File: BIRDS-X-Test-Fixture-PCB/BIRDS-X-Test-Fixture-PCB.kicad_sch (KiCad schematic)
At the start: 0 parts

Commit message: Done test fixture schematic
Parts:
- added D201, D202: LED, LED_SMD:LED_0603_1608Metric, symbol Device:LED
- added H101, H102, H103, H104, H105, H106, H107: MountingHole_Pad, symbol Mechanical:MountingHole_Pad
- added J101 (x2): ~, Connector_PinHeader_2.00mm:PinHeader_2x25_P2.00mm_Vertical, symbol Connector_Generic:Conn_02x25_Odd_Even
- added J101: LPC-50M2LG, Connector_PinHeader_2.00mm:PinHeader_2x25_P2.00mm_Horizontal, symbol Connector_Generic:Conn_02x25_Odd_Even
- added J102, J109: Conn_01x05, symbol Connector_Generic:Conn_01x05
- added J105, J106, J107, J108: Screw_Terminal_01x02, symbol Connector:Screw_Terminal_01x02
- added J110, J111: Conn_02x05_Odd_Even, symbol Connector_Generic:Conn_02x05_Odd_Even
- added JP101: Jumper_3_Open, symbol Jumper:Jumper_3_Open
- added R203: 1k, Resistor_SMD:R_0603_1608Metric_Pad0.98x0.95mm_HandSolder, symbol Device:R
- added R204: 2.2k, Resistor_SMD:R_0603_1608Metric_Pad0.98x0.95mm_HandSolder, symbol Device:R
- added SW101, SW102: SW_SPDT, symbol Switch:SW_SPDT
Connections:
- new net: JP101.2 (C), SW101.1 (A), SW102.1 (A)
- new net: D201.2 (A), R203.2
- new net: D202.2 (A), R204.2
- new net +3V3: H104.1, H105.1, J101.25 (Pin_25), J101.25 (Pin_25), J101.25 (Pin_25), J101.26 (Pin_26), J101.26 (Pin_26), J101.26 (Pin_26), J102.5 (Pin_5), J105.2 (Pin_2), J106.2 (Pin_2), J109.5 (Pin_5), J110.7 (Pin_7), J110.8 (Pin_8), J111.7 (Pin_7), J111.8 (Pin_8), JP101.1 (A), R203.1
- new net +5V: H106.1, H107.1, J101.15 (Pin_15), J101.15 (Pin_15), J101.15 (Pin_15), J101.16 (Pin_16), J101.16 (Pin_16), J101.16 (Pin_16), J102.3 (Pin_3), J107.2 (Pin_2), J108.2 (Pin_2), J109.3 (Pin_3), J110.10 (Pin_10), J110.9 (Pin_9), J111.10 (Pin_10), J111.9 (Pin_9), JP101.3 (B), R204.1
- new net DIO1_3V3_EN_FROM_BOSS: J101.19 (Pin_19), J101.19 (Pin_19), J101.19 (Pin_19), SW101.2 (B)
- new net DIO2_5V_EN_FROM_BOSS: J101.20 (Pin_20), J101.20 (Pin_20), J101.20 (Pin_20), SW102.2 (B)
- new net GND: D201.1 (K), D202.1 (K), H101.1, H102.1, H103.1, J101.13 (Pin_13), J101.13 (Pin_13), J101.13 (Pin_13), J101.14 (Pin_14), J101.14 (Pin_14), J101.14 (Pin_14), J102.4 (Pin_4), J105.1 (Pin_1), J106.1 (Pin_1), J107.1 (Pin_1), J108.1 (Pin_1), J109.4 (Pin_4), J110.5 (Pin_5), J110.6 (Pin_6), J111.5 (Pin_5), J111.6 (Pin_6), SW101.3 (C), SW102.3 (C)
- new net ST_RST: J101.3 (Pin_3), J101.3 (Pin_3), J101.3 (Pin_3), J110.1 (Pin_1), J111.1 (Pin_1)
- new net ST_SWDCLK: J101.2 (Pin_2), J101.2 (Pin_2), J101.2 (Pin_2), J110.2 (Pin_2), J111.2 (Pin_2)
- new net ST_SWDIO: J101.1 (Pin_1), J101.1 (Pin_1), J101.1 (Pin_1), J110.4 (Pin_4), J111.4 (Pin_4)
- new net SUP_3V3_1: J101.49 (Pin_49), J101.49 (Pin_49), J101.49 (Pin_49), J101.50 (Pin_50), J101.50 (Pin_50), J101.50 (Pin_50)
- new net SUP_UNREG_1: J101.23 (Pin_23), J101.23 (Pin_23), J101.23 (Pin_23), J101.24 (Pin_24), J101.24 (Pin_24), J101.24 (Pin_24)
- new net SUP_UNREG_2: J101.35 (Pin_35), J101.35 (Pin_35), J101.35 (Pin_35), J101.36 (Pin_36), J101.36 (Pin_36), J101.36 (Pin_36)
- new net UART_RX_BOSS_TO_JASPER: J101.17 (Pin_17), J101.17 (Pin_17), J101.17 (Pin_17), J102.2 (Pin_2), J109.2 (Pin_2)
- new net UART_TX_JASPER_TO_BOSS: J101.18 (Pin_18), J101.18 (Pin_18), J101.18 (Pin_18), J102.1 (Pin_1), J109.1 (Pin_1)
- no-connect marks 0 -> 95
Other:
- note added: "3-Pin Programming via Main Header: 1 - PROG_DBG_1 -> ST_SWDIO 2 - PROG_DBG_2 -> ST_SWDCLK 3 - PROG_DBG_3 -> ST_RST"
- note added: "BOSS is on USART2"
- note added: "GND is lablled as GND_SYS pin in ICD"
- note added: "On payload PCB, with connector on left side, top-down, Pin 1 is top-right corner"
- note added: "Registration Chunk on Even Side"
- note added: "Select one of these on Digikey NRPN252PARN-RC or LPC-50M2LG (2mm pitch)"
- note added: "Use SUP_3V3_2 as main power, per ICD"

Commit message: Layout and label PCB
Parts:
- added C401: 100n, Capacitor_SMD:C_1206_3216Metric_Pad1.33x1.80mm_HandSolder, symbol Device:C
- added H1, H2, H3, H4: MountingHole, MountingHole:MountingHole_4mm, symbol Mechanical:MountingHole
- added J105: Conn_01x06, Connector_PinHeader_2.54mm:PinHeader_1x06_P2.54mm_Vertical, symbol Connector_Generic:Conn_01x06
- added SW401: SW_Push, Button_Switch_THT:SW_PUSH_6mm, symbol Switch:SW_Push
- D201, D202: footprint LED_SMD:LED_0603_1608Metric -> LED_SMD:LED_1206_3216Metric_Pad1.42x1.75mm_HandSolder
- H_3V3_1: renamed from H104; footprint (none) -> MountingHole:MountingHole_4mm_Pad_Via
- H_3V3_2: renamed from H105; footprint (none) -> MountingHole:MountingHole_4mm_Pad_Via
- H_5V_1: renamed from H106; footprint (none) -> MountingHole:MountingHole_4mm_Pad_Via
- H_5V_2: renamed from H107; footprint (none) -> MountingHole:MountingHole_4mm_Pad_Via
- H_GND_1: renamed from H101; footprint (none) -> MountingHole:MountingHole_4mm_Pad_Via
- H_GND_2: renamed from H102; footprint (none) -> MountingHole:MountingHole_4mm_Pad_Via
- H_GND_3: renamed from H103; footprint (none) -> MountingHole:MountingHole_4mm_Pad_Via
- J101: footprint Connector_PinHeader_2.00mm:PinHeader_2x25_P2.00mm_Vertical -> Connector_PinHeader_2.54mm:PinHeader_2x25_P2.54mm_Vertical
- J102, J109: footprint (none) -> Connector_PinHeader_2.54mm:PinHeader_1x05_P2.54mm_Vertical
- J110, J111: footprint (none) -> Connector_IDC:IDC-Header_2x05_P2.54mm_Latch_Vertical
- JP101: footprint (none) -> Connector_PinHeader_2.54mm:PinHeader_1x03_P2.54mm_Vertical
- J_3V3_1: renamed from J105; footprint (none) -> TerminalBlock:TerminalBlock_bornier-2_P5.08mm
- J_3V3_2: renamed from J106; footprint (none) -> TerminalBlock:TerminalBlock_bornier-2_P5.08mm
- J_5V_1: renamed from J107; footprint (none) -> TerminalBlock:TerminalBlock_bornier-2_P5.08mm
- J_5V_2: renamed from J108; footprint (none) -> TerminalBlock:TerminalBlock_bornier-2_P5.08mm
- R203, R204: footprint Resistor_SMD:R_0603_1608Metric_Pad0.98x0.95mm_HandSolder -> Resistor_THT:R_Axial_DIN0411_L9.9mm_D3.6mm_P12.70mm_Horizontal
- SW_3V3_EN_DIO1: renamed from SW101; footprint (none) -> Button_Switch_THT:SW_Slide_1P2T_CK_OS102011MS2Q
- SW_5V_EN_DIO2: renamed from SW102; footprint (none) -> Button_Switch_THT:SW_Slide_1P2T_CK_OS102011MS2Q
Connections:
- net +3V3: now also J105.1 (Pin_1), J105.4 (Pin_4)
- net DIO1_3V3_EN_FROM_BOSS: now also J105.2 (Pin_2)
- net DIO2_5V_EN_FROM_BOSS: now also J105.5 (Pin_5)
- net GND: now also C401.2, J105.3 (Pin_3), J105.6 (Pin_6), SW401.1
- net ST_RST: now also C401.1, SW401.2
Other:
- note added: "Registration Chunk on Odd Side"
- note added: "Reset Button"
- note removed: "Registration Chunk on Even Side"
- moved on the sheet: J110, J111, J_3V3_1, J_3V3_2, J_5V_1, J_5V_2

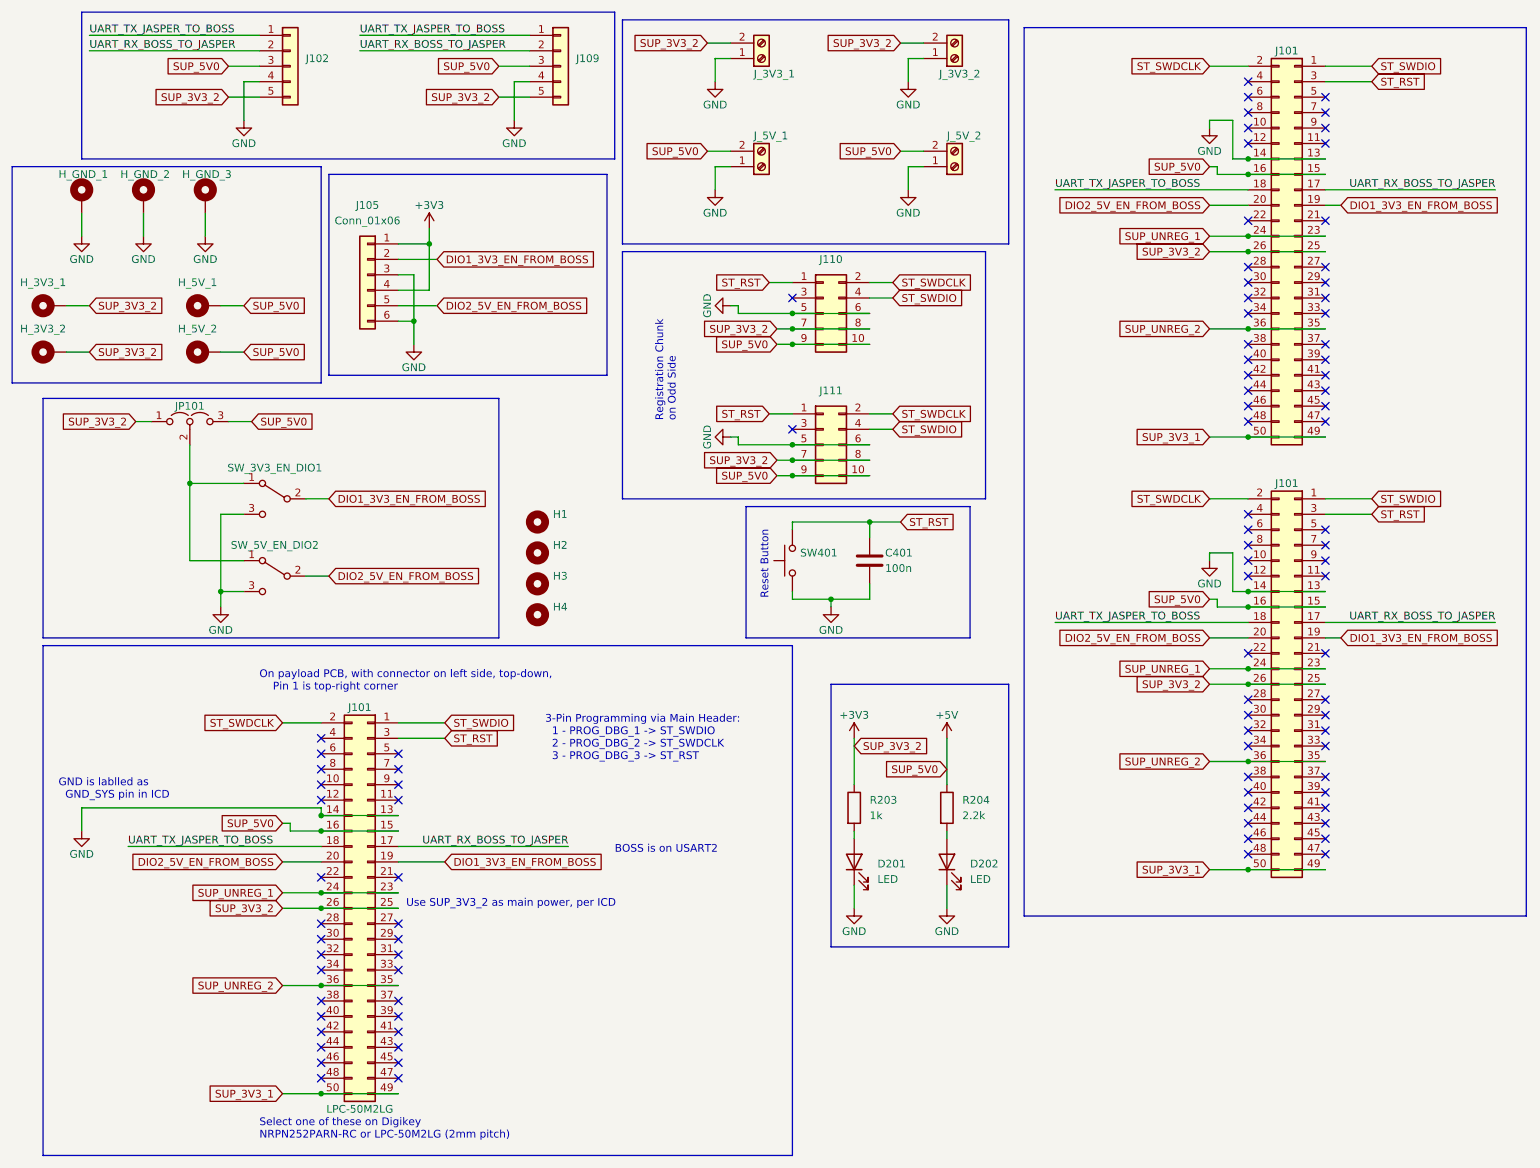
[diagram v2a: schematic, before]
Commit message: Finish test fixture
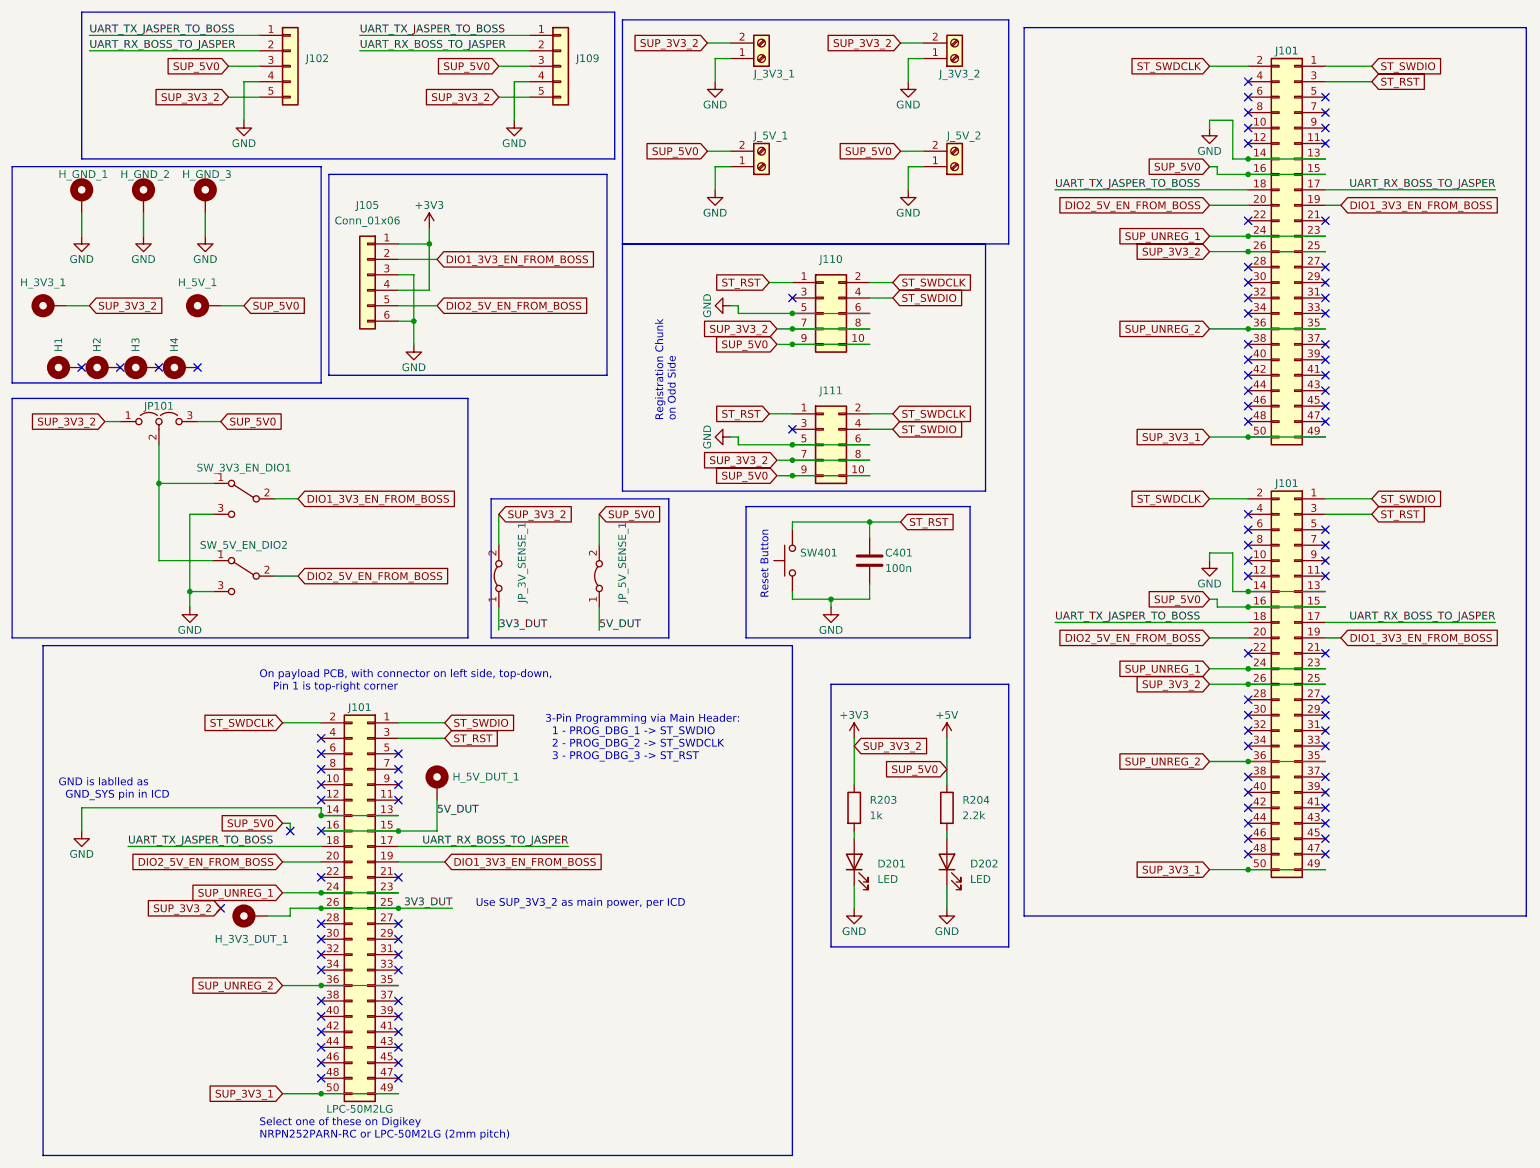
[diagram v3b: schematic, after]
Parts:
- removed H_3V3_2, H_5V_2: MountingHole_Pad, MountingHole:MountingHole_4mm_Pad_Via, symbol Mechanical:MountingHole_Pad
- added H_3V3_DUT_1, H_5V_DUT_1: MountingHole_Pad, MountingHole:MountingHole_4mm_Pad_Via, symbol Mechanical:MountingHole_Pad
- added JP_3V_SENSE_1, JP_5V_SENSE_1: Jumper_2_Bridged, TestPoint:TestPoint_2Pads_Pitch2.54mm_Drill0.8mm, symbol Jumper:Jumper_2_Bridged
- H1, H2, H3, H4: footprint MountingHole:MountingHole_4mm -> MountingHole:MountingHole_4mm_Pad; symbol Mechanical:MountingHole -> Mechanical:MountingHole_Pad
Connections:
- net +3V3: now also JP_3V_SENSE_1.2 (B); no longer J101.25 (Pin_25), J101.26 (Pin_26)
- net +5V: now also JP_5V_SENSE_1.2 (B); no longer J101.15 (Pin_15), J101.16 (Pin_16)
- new net 3V3_DUT: H_3V3_DUT_1.1, J101.25 (Pin_25), J101.26 (Pin_26), JP_3V_SENSE_1.1 (A)
- new net 5V_DUT: H_5V_DUT_1.1, J101.15 (Pin_15), J101.16 (Pin_16), JP_5V_SENSE_1.1 (A)
- no-connect marks 95 -> 102
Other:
- note removed: "BOSS is on USART2"
- moved on the sheet: JP101, SW_3V3_EN_DIO1, SW_5V_EN_DIO2

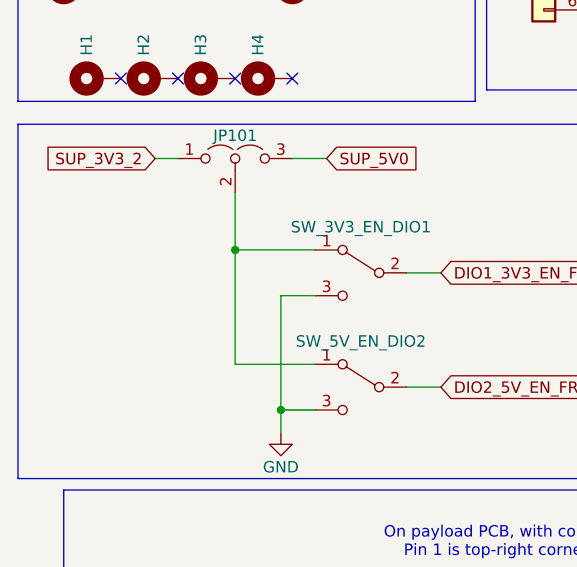
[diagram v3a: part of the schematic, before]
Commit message: Add resistors to switch part
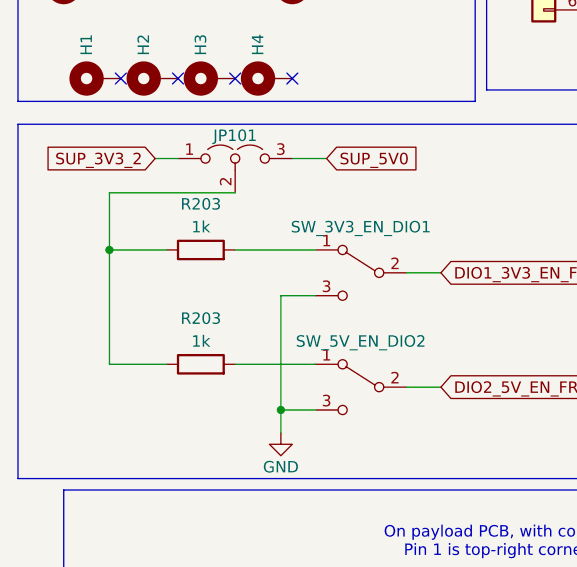
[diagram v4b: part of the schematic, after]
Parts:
- added R203 (x2): 1k, Resistor_THT:R_Axial_DIN0411_L9.9mm_D3.6mm_P12.70mm_Horizontal, symbol Device:R
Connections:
- new net: JP101.2 (C), R203.1, R203.1
- new net: R203.2, SW_3V3_EN_DIO1.1 (A)
- new net: R203.2, SW_5V_EN_DIO2.1 (A)
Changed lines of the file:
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@@
   (junction (at 43.18 107.95) (diameter 0) (color 0 0 0 0)
   )
-  (junction (at 38.1 90.17) (diameter 0) (color 0 0 0 0)
-  )
   (junction (at 77.47 160.02) (diameter 0) (color 0 0 0 0)
   )
@@
   )
   (junction (at 80.01 63.5) (diameter 0) (color 0 0 0 0)
+  )
+  (junction (at 24.13 90.17) (diameter 0) (color 0 0 0 0)
   )
   (junction (at 217.17 107.95) (diameter 0) (color 0 0 0 0)
@@
     (stroke (width 0) (type default))
   )
+  (wire (pts (xy 38.1 83.82) (xy 24.13 83.82))
+    (stroke (width 0) (type default))
+  )
   (wire (pts (xy 83.82 142.24) (xy 83.82 147.32))
     (stroke (width 0) (type default))
@@
     (stroke (width 0) (type default))
   )
+  (wire (pts (xy 24.13 90.17) (xy 24.13 102.87))
+    (stroke (width 0) (type default))
+  )
   (wire (pts (xy 212.09 38.1) (xy 212.09 39.37))
     (stroke (width 0) (type default))
@@
     (stroke (width 0) (type default))
   )
-  (wire (pts (xy 38.1 102.87) (xy 38.1 90.17))
-    (stroke (width 0) (type default))
-  )
   (wire (pts (xy 52.07 60.96) (xy 48.26 60.96))
     (stroke (width 0) (type default))
@@
     (stroke (width 0) (type default))
   )
+  (wire (pts (xy 24.13 83.82) (xy 24.13 90.17))
+    (stroke (width 0) (type default))
+  )
   (wire (pts (xy 161.29 38.1) (xy 163.83 38.1))
     (stroke (width 0) (type default))
@@
     (stroke (width 0) (type default))
   )
+  (wire (pts (xy 24.13 102.87) (xy 30.48 102.87))
+    (stroke (width 0) (type default))
+  )
   (wire (pts (xy 229.87 44.45) (xy 232.41 44.45))
     (stroke (width 0) (type default))
@@
     (stroke (width 0) (type default))
   )
+  (wire (pts (xy 38.1 90.17) (xy 46.99 90.17))
+    (stroke (width 0) (type default))
+  )
   (wire (pts (xy 71.12 19.05) (xy 99.06 19.05))
     (stroke (width 0) (type default))
@@
     (stroke (width 0) (type default))
   )
-  (wire (pts (xy 38.1 90.17) (xy 46.99 90.17))
-    (stroke (width 0) (type default))
-  )
   (wire (pts (xy 229.87 41.91) (xy 257.81 41.91))
     (stroke (width 0) (type default))
@@
     (stroke (width 0) (type default))
   )
+  (wire (pts (xy 24.13 90.17) (xy 30.48 90.17))
+    (stroke (width 0) (type default))
+  )
   (wire (pts (xy 152.4 156.21) (xy 152.4 160.02))
     (stroke (width 0) (type default))
@@
   )
   (wire (pts (xy 77.47 152.4) (xy 85.09 152.4))
-    (stroke (width 0) (type default))
-  )
-  (wire (pts (xy 38.1 83.82) (xy 38.1 90.17))
     (stroke (width 0) (type default))
   )
@@
         (path "/f4adf4d7-bfd7-45f2-804f-a54aa4165d06"
           (reference "#PWR0104") (unit 1)
+        )
+      )
+    )
+  )
+  (symbol (lib_id "Device:R") (at 34.29 90.17 90) (unit 1)
+    (in_bom yes) (on_board yes) (dnp no)
+    (property "Reference" "R203" (at 34.29 85.09 90)
+      (effects (font (size 1.27 1.27)))
+    )
+    (property "Value" "1k" (at 34.29 87.63 90)
+      (effects (font (size 1.27 1.27)))
+    )
+    (property "Footprint" "Resistor_THT:R_Axial_DIN0411_L9.9mm_D3.6mm_P12.70mm_Horizontal" (at 34.29 91.948 90)
+      (effects (font (size 1.27 1.27)) hide)
+    )
+    (property "Datasheet" "~" (at 34.29 90.17 0)
+      (effects (font (size 1.27 1.27)) hide)
+    )
+    (pin "1")
+    (pin "2")
+    (instances
+      (project "BIRDS-X-PCB"
+        (path "/c2796b15-795a-4d6e-ad4b-0ba87ded4bc9/f0b1214b-f453-423f-b2cf-f5d10e08eafe"
+          (reference "R203") (unit 1)
+        )
+      )
+      (project "BIRDS-X-Test-Fixture-PCB"
+        (path "/f4adf4d7-bfd7-45f2-804f-a54aa4165d06"
+          (reference "R102") (unit 1)
         )
       )
@@
         )
       )
+    )
+  )
+  (symbol (lib_id "Device:R") (at 34.29 102.87 90) (unit 1)
+    (in_bom yes) (on_board yes) (dnp no)
+    (property "Reference" "R203" (at 34.29 97.79 90)
+      (effects (font (size 1.27 1.27)))
+    )
+    (property "Value" "1k" (at 34.29 100.33 90)
+      (effects (font (size 1.27 1.27)))
+    )
+    (property "Footprint" "Resistor_THT:R_Axial_DIN0411_L9.9mm_D3.6mm_P12.70mm_Horizontal" (at 34.29 104.648 90)
+      (effects (font (size 1.27 1.27)) hide)
+    )
+    (property "Datasheet" "~" (at 34.29 102.87 0)
+      (effects (font (size 1.27 1.27)) hide)
+    )
+    (pin "1")
+    (pin "2")
+    (instances
+      (project "BIRDS-X-PCB"
+        (path "/c2796b15-795a-4d6e-ad4b-0ba87ded4bc9/f0b1214b-f453-423f-b2cf-f5d10e08eafe"
+          (reference "R203") (unit 1)
+        )
+      )
+      (project "BIRDS-X-Test-Fixture-PCB"
+        (path "/f4adf4d7-bfd7-45f2-804f-a54aa4165d06"
+          (reference "R101") (unit 1)
+        )
+      )
